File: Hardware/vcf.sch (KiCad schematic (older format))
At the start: 67 parts, among them U1 TL074, U2 TL074, U3 TL074

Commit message: fix some bias voltage issues in the LFO schematic. Also begin working on envelope firmware, but this is in progress.
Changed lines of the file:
@@
 	2200 1300 2350 1300
 Wire Wire Line
-	800  1100 1000 1100
-Wire Wire Line
-	1000 1100 1100 1100
+	800  1100 1100 1100
 Connection ~ 3100 1200
 Wire Wire Line
@@
 Connection ~ 2100 1100
 Wire Wire Line
-	1850 1100 2100 1100
-Wire Wire Line
-	2100 1100 2350 1100
-Wire Wire Line
-	2950 1200 3100 1200
-Wire Wire Line
-	3100 1200 3200 1200
+	1850 1100 2350 1100
+Wire Wire Line
+	2950 1200 3200 1200
 Wire Wire Line
 	3050 2200 3050 2700
@@
 	1000 2100 1650 2100
 Wire Wire Line
-	1850 2100 1950 2100
-Wire Wire Line
-	1950 2100 2300 2100
-Wire Wire Line
-	2900 2200 3050 2200
-Wire Wire Line
-	3050 2200 3150 2200
+	1850 2100 2300 2100
+Wire Wire Line
+	2900 2200 3150 2200
 Connection ~ 1000 1100
 Wire Wire Line
-	3950 1200 4150 1200
-Wire Wire Line
-	4150 1200 4450 1200
-Wire Wire Line
-	4450 1200 4550 1200
+	3950 1200 4550 1200
 Connection ~ 4150 1200
 Wire Wire Line
 	4700 650  4450 650
 Wire Wire Line
-	4450 500  4450 650
-Wire Wire Line
-	4450 650  4450 1200
+	4450 500  4450 1200
 Connection ~ 4450 1200
 Wire Wire Line
 	5000 650  5250 650
 Wire Wire Line
-	5250 500  5250 650
-Wire Wire Line
-	5250 650  5250 1300
-Wire Wire Line
-	5600 1300 5750 1300
-Wire Wire Line
-	5750 1300 5900 1300
+	5250 500  5250 1300
+Wire Wire Line
+	5600 1300 5900 1300
 Wire Wire Line
 	4400 1450 4400 1400
@@
 	1000 2100 1000 1100
 Wire Wire Line
-	1400 1100 1500 1100
-Wire Wire Line
-	1500 1100 1650 1100
+	1400 1100 1650 1100
 Connection ~ 1500 1100
 Wire Wire Line
-	5150 1300 5250 1300
-Wire Wire Line
-	5250 1300 5400 1300
+	5150 1300 5400 1300
 Connection ~ 5250 1300
 Wire Wire Line
-	3400 1200 3550 1200
-Wire Wire Line
-	3550 1200 3650 1200
+	3400 1200 3650 1200
 Wire Wire Line
 	3550 1500 3550 1200
 Connection ~ 3550 1200
 Wire Wire Line
-	3350 2200 3550 2200
-Wire Wire Line
-	3550 2200 3650 2200
+	3350 2200 3650 2200
 Wire Wire Line
 	3550 1800 3550 2200
@@
 	2200 3500 2350 3500
 Wire Wire Line
-	800  3300 1000 3300
-Wire Wire Line
-	1000 3300 1100 3300
+	800  3300 1100 3300
 Connection ~ 3100 3400
 Wire Wire Line
@@
 Connection ~ 2100 3300
 Wire Wire Line
-	1850 3300 2100 3300
-Wire Wire Line
-	2100 3300 2350 3300
-Wire Wire Line
-	2950 3400 3100 3400
-Wire Wire Line
-	3100 3400 3200 3400
+	1850 3300 2350 3300
+Wire Wire Line
+	2950 3400 3200 3400
 Wire Wire Line
 	3050 4400 3050 4900
@@
 	1000 4300 1650 4300
 Wire Wire Line
-	1850 4300 1950 4300
-Wire Wire Line
-	1950 4300 2300 4300
-Wire Wire Line
-	2900 4400 3050 4400
-Wire Wire Line
-	3050 4400 3150 4400
+	1850 4300 2300 4300
+Wire Wire Line
+	2900 4400 3150 4400
 Connection ~ 1000 3300
 Wire Wire Line
-	3950 3400 4150 3400
-Wire Wire Line
-	4150 3400 4450 3400
-Wire Wire Line
-	4450 3400 4550 3400
+	3950 3400 4550 3400
 Connection ~ 4150 3400
 Wire Wire Line
 	4700 2850 4450 2850
 Wire Wire Line
-	4450 2600 4450 2850
-Wire Wire Line
-	4450 2850 4450 3400
+	4450 2600 4450 3400
 Connection ~ 4450 3400
 Wire Wire Line
 	5000 2850 5250 2850
 Wire Wire Line
-	5250 2600 5250 2850
-Wire Wire Line
-	5250 2850 5250 3500
-Wire Wire Line
-	5600 3500 5750 3500
-Wire Wire Line
-	5750 3500 5900 3500
+	5250 2600 5250 3500
+Wire Wire Line
+	5600 3500 5900 3500
 Wire Wire Line
 	4400 3650 4400 3600
@@
 	1000 4300 1000 3300
 Wire Wire Line
-	1400 3300 1500 3300
-Wire Wire Line
-	1500 3300 1650 3300
+	1400 3300 1650 3300
 Connection ~ 1500 3300
 Wire Wire Line
-	5150 3500 5250 3500
-Wire Wire Line
-	5250 3500 5400 3500
+	5150 3500 5400 3500
 Connection ~ 5250 3500
 Wire Wire Line
-	3400 3400 3550 3400
-Wire Wire Line
-	3550 3400 3650 3400
+	3400 3400 3650 3400
 Wire Wire Line
 	3550 3700 3550 3400
 Connection ~ 3550 3400
 Wire Wire Line
-	3350 4400 3550 4400
-Wire Wire Line
-	3550 4400 3650 4400
+	3350 4400 3650 4400
 Wire Wire Line
 	3550 4000 3550 4400
@@
 	2150 5900 2300 5900
 Wire Wire Line
-	750  5700 950  5700
-Wire Wire Line
-	950  5700 1050 5700
+	750  5700 1050 5700
 Connection ~ 3050 5800
 Wire Wire Line
@@
 Connection ~ 2050 5700
 Wire Wire Line
-	1800 5700 2050 5700
-Wire Wire Line
-	2050 5700 2300 5700
-Wire Wire Line
-	2900 5800 3050 5800
-Wire Wire Line
-	3050 5800 3150 5800
+	1800 5700 2300 5700
+Wire Wire Line
+	2900 5800 3150 5800
 Wire Wire Line
 	3000 6800 3000 7350
@@
 	950  6700 1600 6700
 Wire Wire Line
-	1800 6700 1900 6700
-Wire Wire Line
-	1900 6700 2250 6700
-Wire Wire Line
-	2850 6800 3000 6800
-Wire Wire Line
-	3000 6800 3100 6800
+	1800 6700 2250 6700
+Wire Wire Line
+	2850 6800 3100 6800
 Connection ~ 950  5700
 Wire Wire Line
-	3900 5800 4100 5800
-Wire Wire Line
-	4100 5800 4400 5800
-Wire Wire Line
-	4400 5800 4500 5800
+	3900 5800 4500 5800
 Connection ~ 4100 5800
 Wire Wire Line
 	4650 5250 4400 5250
 Wire Wire Line
-	4400 5000 4400 5250
-Wire Wire Line
-	4400 5250 4400 5800
+	4400 5000 4400 5800
 Connection ~ 4400 5800
 Wire Wire Line
 	4950 5250 5200 5250
 Wire Wire Line
-	5200 5000 5200 5250
-Wire Wire Line
-	5200 5250 5200 5900
-Wire Wire Line
-	5550 5900 5700 5900
-Wire Wire Line
-	5700 5900 5850 5900
+	5200 5000 5200 5900
+Wire Wire Line
+	5550 5900 5850 5900
 Wire Wire Line
 	4350 6050 4350 6000
@@
 	950  6700 950  5700
 Wire Wire Line
-	1350 5700 1450 5700
-Wire Wire Line
-	1450 5700 1600 5700
+	1350 5700 1600 5700
 Connection ~ 1450 5700
 Wire Wire Line
-	5100 5900 5200 5900
-Wire Wire Line
-	5200 5900 5350 5900
+	5100 5900 5350 5900
 Connection ~ 5200 5900
 Wire Wire Line
-	3350 5800 3500 5800
-Wire Wire Line
-	3500 5800 3600 5800
+	3350 5800 3600 5800
 Wire Wire Line
 	3500 6100 3500 5800
 Connection ~ 3500 5800
 Wire Wire Line
-	3300 6800 3500 6800
-Wire Wire Line
-	3500 6800 3600 6800
+	3300 6800 3600 6800
 Wire Wire Line
 	3500 6400 3500 6800
@@
 	6900 4600 7050 4600
 Wire Wire Line
-	5500 4400 5700 4400
-Wire Wire Line
-	5700 4400 5800 4400
+	5500 4400 5800 4400
 Connection ~ 7800 4500
 Wire Wire Line
@@
 Connection ~ 6800 4400
 Wire Wire Line
-	6550 4400 6800 4400
-Wire Wire Line
-	6800 4400 7050 4400
-Wire Wire Line
-	7650 4500 7800 4500
-Wire Wire Line
-	7800 4500 7900 4500
+	6550 4400 7050 4400
+Wire Wire Line
+	7650 4500 7900 4500
 Wire Wire Line
 	7750 5500 7750 6050
@@
 	5700 5400 6350 5400
 Wire Wire Line
-	6550 5400 6650 5400
-Wire Wire Line
-	6650 5400 7000 5400
-Wire Wire Line
-	7600 5500 7750 5500
-Wire Wire Line
-	7750 5500 7850 5500
+	6550 5400 7000 5400
+Wire Wire Line
+	7600 5500 7850 5500
 Connection ~ 5700 4400
 Wire Wire Line
-	8650 4500 8850 4500
-Wire Wire Line
-	8850 4500 9150 4500
-Wire Wire Line
-	9150 4500 9250 4500
+	8650 4500 9250 4500
 Connection ~ 8850 4500
 Wire Wire Line
 	9400 3950 9150 3950
 Wire Wire Line
-	9150 3700 9150 3950
-Wire Wire Line
-	9150 3950 9150 4500
+	9150 3700 9150 4500
 Connection ~ 9150 4500
 Wire Wire Line
 	9700 3950 9950 3950
 Wire Wire Line
-	9950 3700 9950 3950
-Wire Wire Line
-	9950 3950 9950 4600
-Wire Wire Line
-	10300 4600 10450 4600
-Wire Wire Line
-	10450 4600 10600 4600
+	9950 3700 9950 4600
+Wire Wire Line
+	10300 4600 10600 4600
 Wire Wire Line
 	9100 4750 9100 4700
@@
 	5700 5400 5700 4400
 Wire Wire Line
-	6100 4400 6200 4400
-Wire Wire Line
-	6200 4400 6350 4400
+	6100 4400 6350 4400
 Connection ~ 6200 4400
 Wire Wire Line
-	9850 4600 9950 4600
-Wire Wire Line
-	9950 4600 10100 4600
+	9850 4600 10100 4600
 Connection ~ 9950 4600
 Wire Wire Line
-	8100 4500 8250 4500
-Wire Wire Line
-	8250 4500 8350 4500
+	8100 4500 8350 4500
 Wire Wire Line
 	8250 4800 8250 4500
 Connection ~ 8250 4500
 Wire Wire Line
-	8050 5500 8250 5500
-Wire Wire Line
-	8250 5500 8350 5500
+	8050 5500 8350 5500
 Wire Wire Line
 	8250 5100 8250 5500

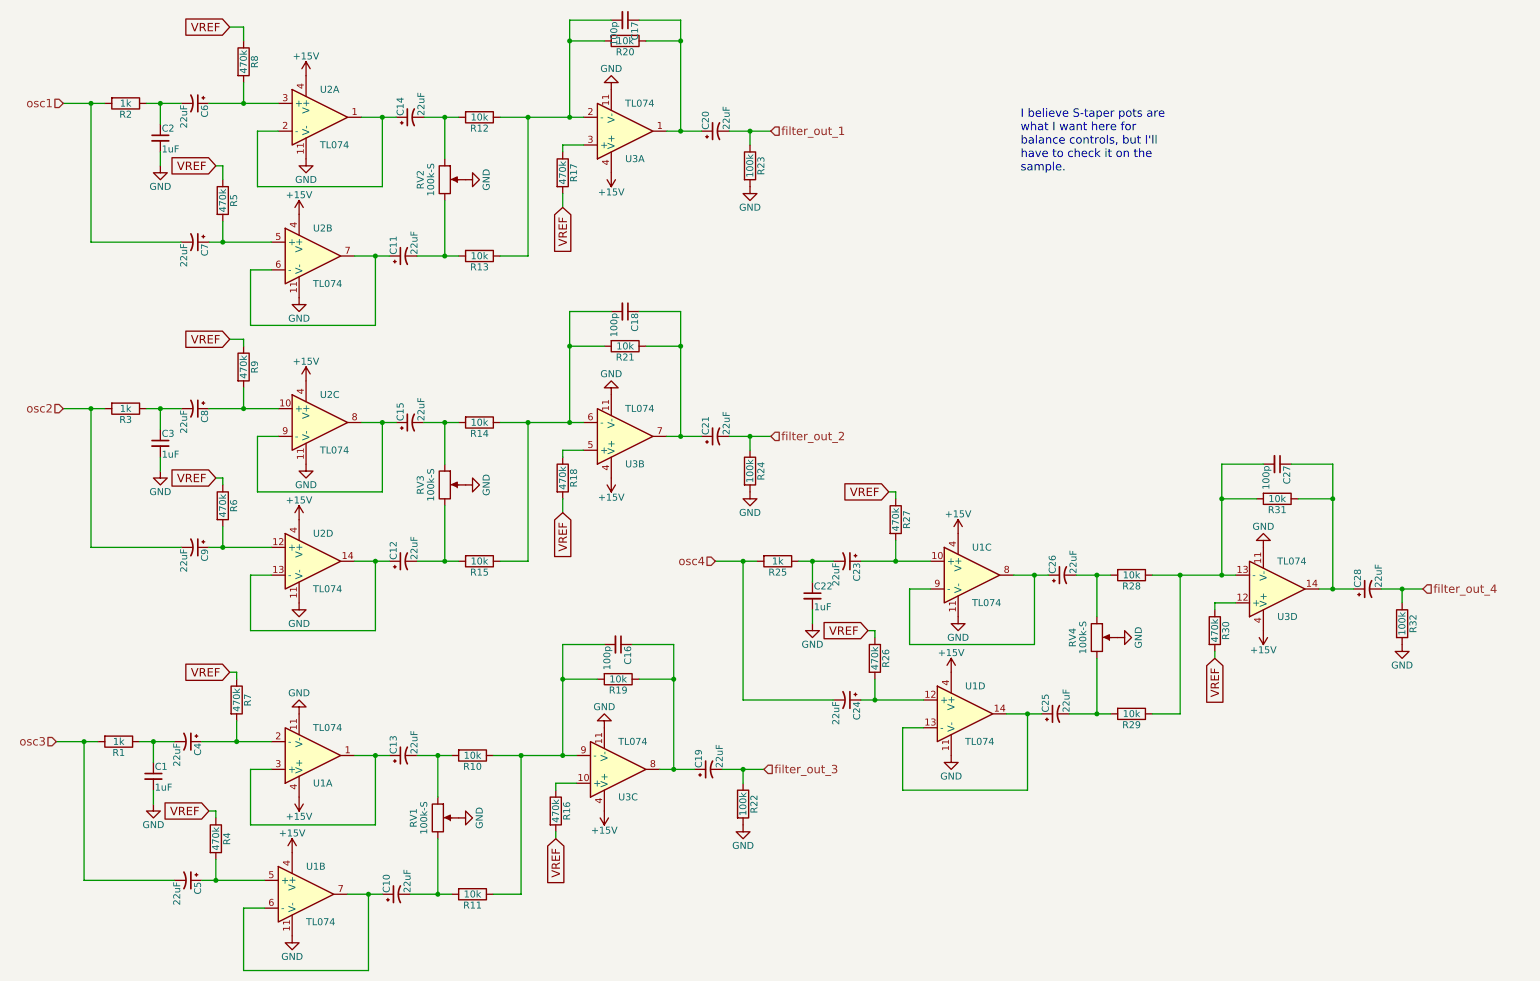
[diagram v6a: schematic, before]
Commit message: change LPF to sallen key filters.
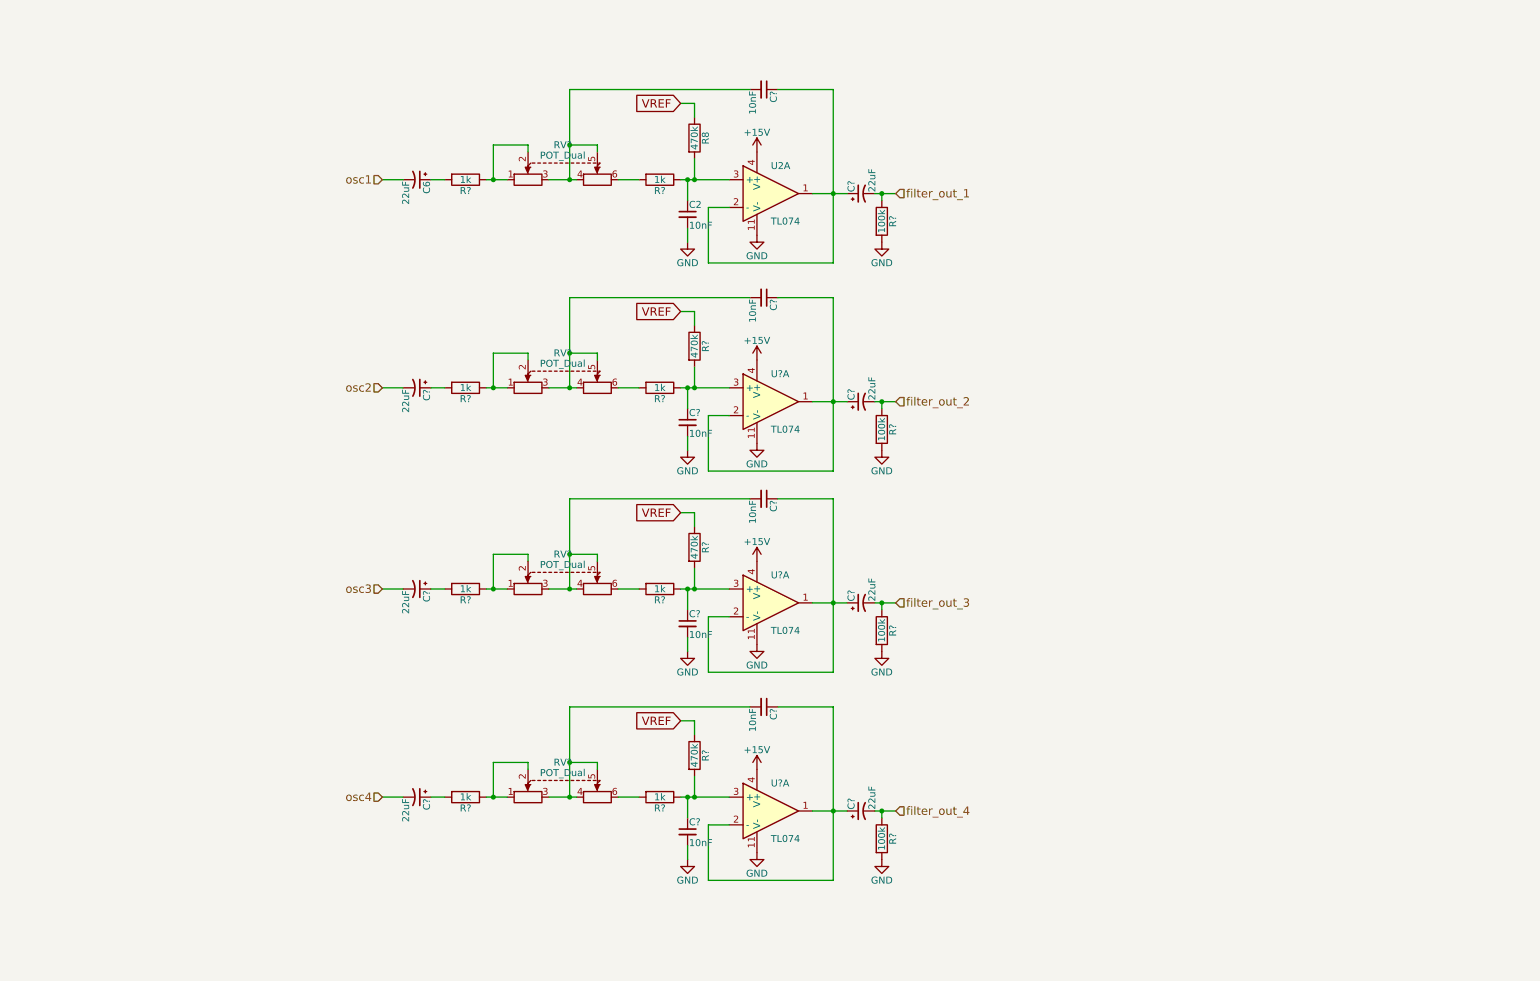
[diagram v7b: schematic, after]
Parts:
- removed C1, C22, C3: 1uF, Capacitors_SMD:CP_Elec_4x4.5, symbol C_Small
- removed C10, C11, C12, C13, C14, C15, C19, C20, C21, C23, C24, C25, C26, C28, C4, C5, C7, C8, C9: 22uF, Capacitors_SMD:CP_Elec_5x5.7, symbol CP1_Small
- removed C16, C17, C18, C27: 100p, digikey-footprints:0805, symbol C_Small
- removed R1, R2, R25, R3: 1k, digikey-footprints:0805, symbol R
- removed R10, R11, R12, R13, R14, R15, R19, R20, R21, R28, R29, R31: 10k, digikey-footprints:0805, symbol R
- removed R16, R17, R18, R26, R27, R30, R4, R5, R6, R7, R9: 470k, digikey-footprints:0805, symbol R
- removed R22, R23, R24, R32: 100k, digikey-footprints:0805, symbol R
- removed RV1, RV2, RV3, RV4: 100k-S, Potentiometers:Potentiometer_Bourns_PTV09A-1_Horizontal, symbol POT
- removed U1, U3: TL074, digikey-footprints:SOIC-14_W3.9mm, symbol TL074
- removed unit 2 of U2
- removed unit 3 of U2
- removed unit 4 of U2
- added C? (x7): 10nF, Capacitors_SMD:CP_Elec_4x4.5, symbol C_Small
- added C? (x7): 22uF, Capacitors_SMD:CP_Elec_5x5.7, symbol CP1_Small
- added R? (x8): 1k, digikey-footprints:0805, symbol R
- added R? (x4): 100k, digikey-footprints:0805, symbol R
- added R? (x3): 470k, digikey-footprints:0805, symbol R
- added RV? (x4): POT_Dual, symbol POT_Dual
- added U? (x3): TL074, digikey-footprints:SOIC-14_W3.9mm, symbol TL074
- C2: value 1uF -> 10nF
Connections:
- net +15V: now also U?.4 (V+), U?.4 (V+), U?.4 (V+)
- net GND: now also C?.2, C?.2, C?.2, R?.2, R?.2, R?.2, R?.2, U?.11 (V-), U?.11 (V-), U?.11 (V-)
- net VREF: now also R?.1, R?.1, R?.1
- net filter_out_1: now also C?.2, R?.1
- net filter_out_2: now also C?.2, R?.1
- net filter_out_3: now also C?.2, R?.1
- net filter_out_4: now also C?.2, R?.1
- net osc1: now also C6.2
- net osc2: now also C?.2
- net osc3: now also C?.2
- net osc4: now also C?.2
- net at C2.1: now also R8.2, U2.3 (+), R?.1; no longer C6.2
- net at U2.1, U2.2 (-): now also C?.1, C?.1
- new net: C6.1, R?.2
- new net: R?.1, RV?.1, RV?.2 (x4)
- new net: R?.2, RV?.6 (x4)
- new net: C?.2, RV?.3, RV?.4, RV?.5 (x4)
- new net: C?.1, C?.1, U?.1, U?.2 (-) (x3)
- new net: C?.1, R?.1, R?.2, U?.3 (+) (x3)
- new net: C?.1, R?.2 (x3)
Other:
- note removed: "I believe S-taper pots are \nwhat I want here for \nbalance controls, but I'll \nhave to check it on the \nsample."
- moved on the sheet: C2, C6, R8, U2A

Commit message: add delay mix control. Currently 50/50 is max possible wet/dry, but this might change.
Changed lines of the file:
@@
 Connection ~ 4450 1650
 Wire Wire Line
-	4450 1000 4450 1400
-Wire Wire Line
-	4450 1400 4450 1650
+	4450 1000 4450 1650
 Wire Wire Line
 	4800 1650 4950 1650
@@
 	4650 1450 4650 1400
 Wire Wire Line
-	4300 1650 4450 1650
-Wire Wire Line
-	4450 1650 4500 1650
+	4300 1650 4500 1650
 Wire Wire Line
 	3250 1650 3100 1650
@@
 	6350 1000 5950 1000
 Wire Wire Line
-	6200 1750 6350 1750
-Wire Wire Line
-	6350 1750 6450 1750
-Wire Wire Line
-	6350 1000 6350 1750
-Wire Wire Line
-	6350 1750 6350 2250
+	6200 1750 6450 1750
+Wire Wire Line
+	6350 1000 6350 2250
 Wire Wire Line
 	6350 2250 5450 2250
@@
 	5250 1100 5350 1100
 Wire Wire Line
-	5250 1650 5300 1650
-Wire Wire Line
-	5300 1650 5350 1650
-Wire Wire Line
-	5350 1650 5600 1650
+	5250 1650 5600 1650
 Connection ~ 5350 1650
 Wire Wire Line
@@
 	3900 1400 3900 1650
 Wire Wire Line
-	3850 1650 3900 1650
-Wire Wire Line
-	3900 1650 4000 1650
+	3850 1650 4000 1650
 Connection ~ 3900 1650
 $Comp
@@
 $EndComp
 Wire Wire Line
-	6800 1750 6700 1750
-Wire Wire Line
-	6700 1750 6650 1750
+	6650 1750 6800 1750
 Wire Wire Line
 	6700 1800 6700 1750
@@
 Connection ~ 4450 3150
 Wire Wire Line
-	4450 2500 4450 2900
-Wire Wire Line
-	4450 2900 4450 3150
+	4450 2500 4450 3150
 Wire Wire Line
 	4800 3150 4950 3150
@@
 	4650 2950 4650 2900
 Wire Wire Line
-	4300 3150 4450 3150
-Wire Wire Line
-	4450 3150 4500 3150
+	4300 3150 4500 3150
 Wire Wire Line
 	3250 3150 3100 3150
@@
 	6350 2500 5950 2500
 Wire Wire Line
-	6200 3250 6350 3250
-Wire Wire Line
-	6350 3250 6450 3250
-Wire Wire Line
-	6350 2500 6350 3250
-Wire Wire Line
-	6350 3250 6350 3750
+	6200 3250 6450 3250
+Wire Wire Line
+	6350 2500 6350 3750
 Wire Wire Line
 	6350 3750 5450 3750
@@
 	5250 2600 5350 2600
 Wire Wire Line
-	5250 3150 5300 3150
-Wire Wire Line
-	5300 3150 5350 3150
-Wire Wire Line
-	5350 3150 5600 3150
+	5250 3150 5600 3150
 Connection ~ 5350 3150
 Wire Wire Line
@@
 	3900 2900 3900 3150
 Wire Wire Line
-	3850 3150 3900 3150
-Wire Wire Line
-	3900 3150 4000 3150
+	3850 3150 4000 3150
 Connection ~ 3900 3150
 $Comp
@@
 $EndComp
 Wire Wire Line
-	6800 3250 6700 3250
-Wire Wire Line
-	6700 3250 6650 3250
+	6650 3250 6800 3250
 Wire Wire Line
 	6700 3300 6700 3250
@@
 Connection ~ 4450 4600
 Wire Wire Line
-	4450 3950 4450 4350
-Wire Wire Line
-	4450 4350 4450 4600
+	4450 3950 4450 4600
 Wire Wire Line
 	4800 4600 4950 4600
@@
 	4650 4400 4650 4350
 Wire Wire Line
-	4300 4600 4450 4600
-Wire Wire Line
-	4450 4600 4500 4600
+	4300 4600 4500 4600
 Wire Wire Line
 	3250 4600 3100 4600
@@
 	6350 3950 5950 3950
 Wire Wire Line
-	6200 4700 6350 4700
-Wire Wire Line
-	6350 4700 6450 4700
-Wire Wire Line
-	6350 3950 6350 4700
-Wire Wire Line
-	6350 4700 6350 5200
+	6200 4700 6450 4700
+Wire Wire Line
+	6350 3950 6350 5200
 Wire Wire Line
 	6350 5200 5450 5200
@@
 	5250 4050 5350 4050
 Wire Wire Line
-	5250 4600 5300 4600
-Wire Wire Line
-	5300 4600 5350 4600
-Wire Wire Line
-	5350 4600 5600 4600
+	5250 4600 5600 4600
 Connection ~ 5350 4600
 Wire Wire Line
@@
 	3900 4350 3900 4600
 Wire Wire Line
-	3850 4600 3900 4600
-Wire Wire Line
-	3900 4600 4000 4600
+	3850 4600 4000 4600
 Connection ~ 3900 4600
 $Comp
@@
 $EndComp
 Wire Wire Line
-	6800 4700 6700 4700
-Wire Wire Line
-	6700 4700 6650 4700
+	6650 4700 6800 4700
 Wire Wire Line
 	6700 4750 6700 4700
@@
 Connection ~ 4450 6100
 Wire Wire Line
-	4450 5450 4450 5850
-Wire Wire Line
-	4450 5850 4450 6100
+	4450 5450 4450 6100
 Wire Wire Line
 	4800 6100 4950 6100
@@
 	4650 5900 4650 5850
 Wire Wire Line
-	4300 6100 4450 6100
-Wire Wire Line
-	4450 6100 4500 6100
+	4300 6100 4500 6100
 Wire Wire Line
 	3250 6100 3100 6100
@@
 	6350 5450 5950 5450
 Wire Wire Line
-	6200 6200 6350 6200
-Wire Wire Line
-	6350 6200 6450 6200
-Wire Wire Line
-	6350 5450 6350 6200
-Wire Wire Line
-	6350 6200 6350 6700
+	6200 6200 6450 6200
+Wire Wire Line
+	6350 5450 6350 6700
 Wire Wire Line
 	6350 6700 5450 6700
@@
 	5250 5550 5350 5550
 Wire Wire Line
-	5250 6100 5300 6100
-Wire Wire Line
-	5300 6100 5350 6100
-Wire Wire Line
-	5350 6100 5600 6100
+	5250 6100 5600 6100
 Connection ~ 5350 6100
 Wire Wire Line
@@
 	3900 5850 3900 6100
 Wire Wire Line
-	3850 6100 3900 6100
-Wire Wire Line
-	3900 6100 4000 6100
+	3850 6100 4000 6100
 Connection ~ 3900 6100
 $Comp
@@
 $EndComp
 Wire Wire Line
-	6800 6200 6700 6200
-Wire Wire Line
-	6700 6200 6650 6200
+	6650 6200 6800 6200
 Wire Wire Line
 	6700 6250 6700 6200
